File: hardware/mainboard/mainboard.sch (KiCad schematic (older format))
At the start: 1 part, among them J1 2309407-1

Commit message: displays done, sd card and camera is left
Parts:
- added C?: 10nF, symbol Device:C_Small
- added C?: 4.7uF, symbol Device:C_Small
- added C?: 10uF, symbol Device:C_Small
- added J?: Micro_SD_Card_Det, symbol Connector:Micro_SD_Card_Det
- added JP? (x2): BL_SELECT, symbol Jumper:SolderJumper_3_Open
- added U?: MCP1725-3302E_SN, SOIC127P599X175-8N, symbol mainboard:MCP1725-3302E_SN
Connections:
- net labels added: GPIO_BL, LED_3V, MIPI_RX0_CLKN, MIPI_RX0_CLKP, MIPI_RX0_D0N, MIPI_RX0_D0P, MIPI_RX0_D1N, MIPI_RX0_D1P, MIPI_RX0_D2N, MIPI_RX0_D2P, MIPI_RX0_D3N, MIPI_RX0_D3P, MIPI_TX0_CLKN, MIPI_TX0_CLKP, MIPI_TX0_D0N, MIPI_TX0_D0P, MIPI_TX0_D1N, MIPI_TX0_D1P, MIPI_TX0_D2N, MIPI_TX0_D2P, MIPI_TX0_D3N, MIPI_TX0_D3P, MIPI_TX1_CLKN, MIPI_TX1_CLKP, MIPI_TX1_D0N, MIPI_TX1_D0P, MIPI_TX1_D1N, MIPI_TX1_D1P, MIPI_TX1_D2N, MIPI_TX1_D2P, MIPI_TX1_D3N, MIPI_TX1_D3P, RESX_0, RESX_1
- wire segments 21 -> 99
- no-connect marks 0 -> 1
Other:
- note added: "HDMI\n"
- note added: "MIPI CSI0"
- note added: "MIPI CSI0\n"
- note added: "MIPI DSI0"
- note added: "MIPI DSI1"
- note added: "MIPI DSI1\n"
- moved on the sheet: J1A, J1B

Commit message: finished camera, sd, imu, power supplies, might be done with schematic
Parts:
- removed C?: 10nF, symbol Device:C_Small
- removed C?: 4.7uF, symbol Device:C_Small
- removed C?: 10uF, symbol Device:C_Small
- removed J?: Micro_SD_Card_Det, symbol Connector:Micro_SD_Card_Det
- removed U?: MCP1725-3302E_SN, SOIC127P599X175-8N, symbol mainboard:MCP1725-3302E_SN
- added C10, C12, C8: 100nF, symbol Device:C_Small
- added C11: 4.7uF, symbol Device:C_Small
- added C13, C6, C7: 1uF, symbol Device:C_Small
- added C9, C?: 10nF, symbol Device:C_Small
- added C? (x2): 0.1uF, symbol Device:C_Small
- added C?: 2.2uF, symbol Device:C_Small
- added J3: Conn_01x02_Male, symbol Connector:Conn_01x02_Male
- added J4: AXK7L24223G, PANASONIC_AXK7L24223G, symbol mainboard:AXK7L24223G
- added J5: 503182-1852, MOLEX_503182-1852, symbol mainboard:503182-1852
- added R1: 60k, symbol Device:R_Small_US
- added R2: 10k, symbol Device:R_Small_US
- added TP1, TP2, TP3, TP4: TestPoint, symbol Connector:TestPoint
- added U2: MIC5504-1.2YM5-TR, SOT23-5P95_280X145XL45X37N, symbol mainboard:MIC5504-1.2YM5-TR
- added U3: MCP1725-ADJE_MC, SOIC127P599X175-8N, symbol mainboard:MCP1725-ADJE_MC
- added U?: ICM-20602, PQFN50P300X300X80-16N, symbol mainboard:ICM-20602
- gave numbers to parts that had none: 2
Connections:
- net labels added: +1V2, +2V8, GPIO2_B3_CIF_CLKOUTA, I2C1_SCL, I2C1_SDA, I2C2_SCL, I2C2_SDA, MIPI_CSI0_PWN, MIPI_CSI1_RST
- net labels removed: LED_3V
- wire segments 99 -> 132
- no-connect marks 1 -> 5
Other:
- note added: "(this is hella sus)"
- note added: "Camera digital core regulator\n"
- note added: "OV13850 B2B Conn\n"
- note added: "microSD\n"
- moved on the sheet: J1B

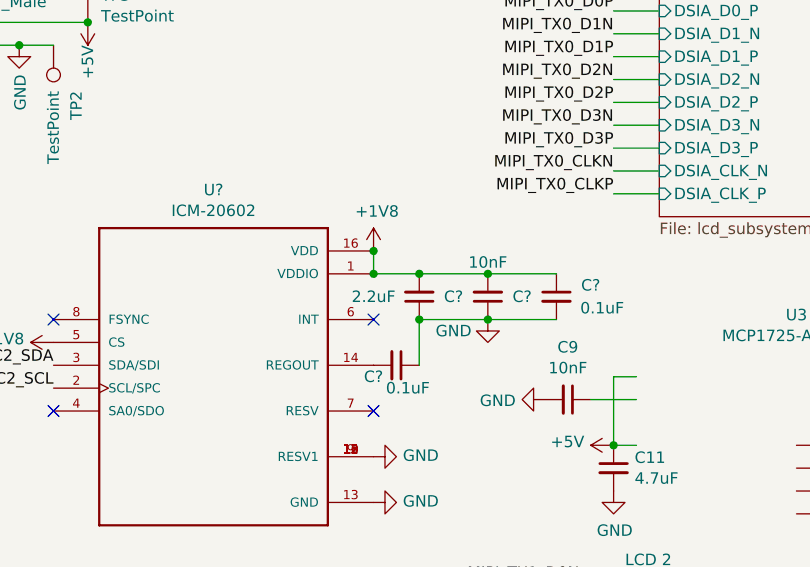
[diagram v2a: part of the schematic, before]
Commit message: footprints assigned, ready to begin pcb design
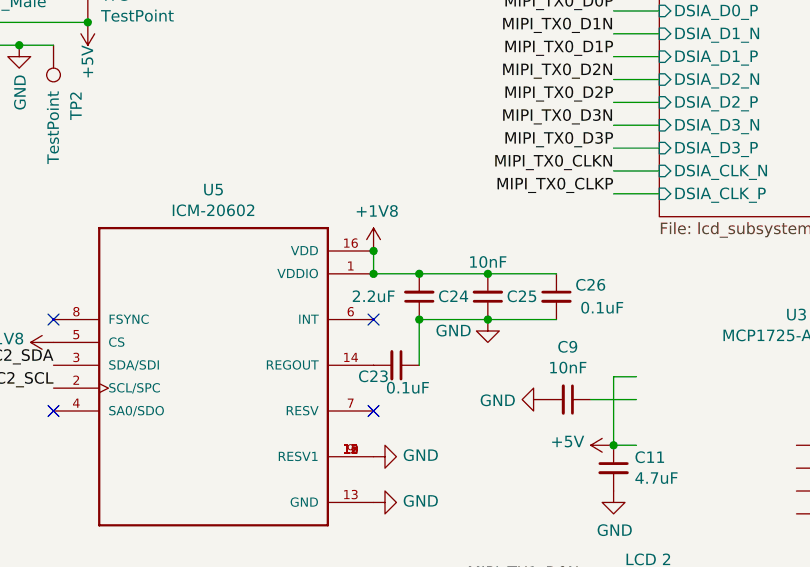
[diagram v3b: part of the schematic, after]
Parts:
- C10, C11, C12, C13, C6, C7, C8, C9: footprint (none) -> Capacitor_SMD:C_0603_1608Metric_Pad1.08x0.95mm_HandSolder
- C23, C24, C25, C26: renamed from C?; footprint (none) -> Capacitor_SMD:C_0603_1608Metric_Pad1.08x0.95mm_HandSolder
- J3: footprint (none) -> Connector_PinHeader_2.54mm:PinHeader_1x02_P2.54mm_Vertical
- J4: footprint PANASONIC_AXK7L24223G -> mainboard:PANASONIC_AXK7L24223G
- J5: footprint MOLEX_503182-1852 -> mainboard:MOLEX_503182-1852
- JP1, JP2: footprint (none) -> Jumper:SolderJumper-3_P1.3mm_Open_Pad1.0x1.5mm
- R1, R2: footprint (none) -> Resistor_SMD:R_0603_1608Metric_Pad0.98x0.95mm_HandSolder
- TP1, TP2, TP3, TP4: footprint (none) -> TestPoint:TestPoint_Pad_2.5x2.5mm
- U2: footprint SOT23-5P95_280X145XL45X37N -> mainboard:SOT23-5P95_280X145XL45X37N
- U3: footprint SOIC127P599X175-8N -> mainboard:SOIC127P599X175-8N
- U5: renamed from U?; footprint PQFN50P300X300X80-16N -> mainboard:PQFN50P300X300X80-16N
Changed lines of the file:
@@
 F 0 "JP1" V 10754 1318 50  0000 L CNN
 F 1 "BL_SELECT" V 10845 1318 50  0000 L CNN
-F 2 "" H 10800 1250 50  0001 C CNN
+F 2 "Jumper:SolderJumper-3_P1.3mm_Open_Pad1.0x1.5mm" H 10800 1250 50  0001 C CNN
 F 3 "~" H 10800 1250 50  0001 C CNN
 	1    10800 1250
@@
 F 0 "JP2" V 10604 3918 50  0000 L CNN
 F 1 "BL_SELECT" V 10695 3918 50  0000 L CNN
-F 2 "" H 10650 3850 50  0001 C CNN
+F 2 "Jumper:SolderJumper-3_P1.3mm_Open_Pad1.0x1.5mm" H 10650 3850 50  0001 C CNN
 F 3 "~" H 10650 3850 50  0001 C CNN
 	1    10650 3850
@@
 F 0 "J5" H 10580 5696 50  0000 L CNN
 F 1 "503182-1852" H 10580 5605 50  0000 L CNN
-F 2 "MOLEX_503182-1852" H 10050 5650 50  0001 L BNN
+F 2 "mainboard:MOLEX_503182-1852" H 10050 5650 50  0001 L BNN
 F 3 "Molex" H 10050 5650 50  0001 L BNN
 	1    10050 5650
@@
 F 0 "J4" H 7700 6217 50  0000 C CNN
 F 1 "AXK7L24223G" H 7700 6126 50  0000 C CNN
-F 2 "PANASONIC_AXK7L24223G" H 7700 5450 50  0001 L BNN
+F 2 "mainboard:PANASONIC_AXK7L24223G" H 7700 5450 50  0001 L BNN
 F 3 "Panasonic" H 7700 5450 50  0001 L BNN
 	1    7700 5450
@@
 F 0 "U3" H 9900 3170 50  0000 C CNN
 F 1 "MCP1725-ADJE_MC" H 9900 3079 50  0000 C CNN
-F 2 "SOIC127P599X175-8N" H 9900 2600 50  0001 L BNN
+F 2 "mainboard:SOIC127P599X175-8N" H 9900 2600 50  0001 L BNN
 F 3 "" H 9900 2600 50  0001 C CNN
 	1    9900 2600
@@
 F 0 "C9" V 8671 2400 50  0000 C CNN
 F 1 "10nF" V 8762 2400 50  0000 C CNN
-F 2 "" H 8900 2400 50  0001 C CNN
+F 2 "Capacitor_SMD:C_0603_1608Metric_Pad1.08x0.95mm_HandSolder" H 8900 2400 50  0001 C CNN
 F 3 "~" H 8900 2400 50  0001 C CNN
 	1    8900 2400
@@
 F 0 "C11" H 9192 2746 50  0000 L CNN
 F 1 "4.7uF" H 9192 2655 50  0000 L CNN
-F 2 "" H 9100 2700 50  0001 C CNN
+F 2 "Capacitor_SMD:C_0603_1608Metric_Pad1.08x0.95mm_HandSolder" H 9100 2700 50  0001 C CNN
 F 3 "~" H 9100 2700 50  0001 C CNN
 	1    9100 2700
@@
 F 0 "C13" H 10650 2350 50  0000 C CNN
 F 1 "1uF" H 10650 2250 50  0000 C CNN
-F 2 "" H 10800 2300 50  0001 C CNN
+F 2 "Capacitor_SMD:C_0603_1608Metric_Pad1.08x0.95mm_HandSolder" H 10800 2300 50  0001 C CNN
 F 3 "~" H 10800 2300 50  0001 C CNN
 	1    10800 2300
@@
 F 0 "C8" H 8692 4846 50  0000 L CNN
 F 1 "100nF" H 8692 4755 50  0000 L CNN
-F 2 "" H 8600 4800 50  0001 C CNN
+F 2 "Capacitor_SMD:C_0603_1608Metric_Pad1.08x0.95mm_HandSolder" H 8600 4800 50  0001 C CNN
 F 3 "~" H 8600 4800 50  0001 C CNN
 	1    8600 4800
@@
 F 0 "C10" H 9092 4846 50  0000 L CNN
 F 1 "100nF" H 9092 4755 50  0000 L CNN
-F 2 "" H 9000 4800 50  0001 C CNN
+F 2 "Capacitor_SMD:C_0603_1608Metric_Pad1.08x0.95mm_HandSolder" H 9000 4800 50  0001 C CNN
 F 3 "~" H 9000 4800 50  0001 C CNN
 	1    9000 4800
@@
 F 0 "C12" H 10842 5296 50  0000 L CNN
 F 1 "100nF" H 10842 5205 50  0000 L CNN
-F 2 "" H 10750 5250 50  0001 C CNN
+F 2 "Capacitor_SMD:C_0603_1608Metric_Pad1.08x0.95mm_HandSolder" H 10750 5250 50  0001 C CNN
 F 3 "~" H 10750 5250 50  0001 C CNN
 	1    10750 5250
@@
 F 0 "R1" H 10768 2596 50  0000 L CNN
 F 1 "60k" H 10768 2505 50  0000 L CNN
-F 2 "" H 10700 2550 50  0001 C CNN
+F 2 "Resistor_SMD:R_0603_1608Metric_Pad0.98x0.95mm_HandSolder" H 10700 2550 50  0001 C CNN
 F 3 "~" H 10700 2550 50  0001 C CNN
 	1    10700 2550
@@
 F 0 "R2" H 10768 2796 50  0000 L CNN
 F 1 "10k" H 10768 2705 50  0000 L CNN
-F 2 "" H 10700 2750 50  0001 C CNN
+F 2 "Resistor_SMD:R_0603_1608Metric_Pad0.98x0.95mm_HandSolder" H 10700 2750 50  0001 C CNN
 F 3 "~" H 10700 2750 50  0001 C CNN
 	1    10700 2750
@@
 F 0 "J3" H 6308 931 50  0000 C CNN
 F 1 "Conn_01x02_Male" H 6308 840 50  0000 C CNN
-F 2 "" H 6200 750 50  0001 C CNN
+F 2 "Connector_PinHeader_2.54mm:PinHeader_1x02_P2.54mm_Vertical" H 6200 750 50  0001 C CNN
 F 3 "~" H 6200 750 50  0001 C CNN
 	1    6200 750
@@
 F 0 "U2" H 7250 4467 50  0000 C CNN
 F 1 "MIC5504-1.2YM5-TR" H 7250 4376 50  0000 C CNN
-F 2 "SOT23-5P95_280X145XL45X37N" H 7250 4000 50  0001 L BNN
+F 2 "mainboard:SOT23-5P95_280X145XL45X37N" H 7250 4000 50  0001 L BNN
 F 3 "MICREL" H 7250 4000 50  0001 L BNN
 	1    7250 4000
@@
 F 0 "C6" H 7500 3700 50  0000 C CNN
 F 1 "1uF" H 7650 3700 50  0000 C CNN
-F 2 "" H 7800 3700 50  0001 C CNN
+F 2 "Capacitor_SMD:C_0603_1608Metric_Pad1.08x0.95mm_HandSolder" H 7800 3700 50  0001 C CNN
 F 3 "~" H 7800 3700 50  0001 C CNN
 	1    7800 3700
@@
 F 0 "C7" H 7750 4150 50  0000 C CNN
 F 1 "1uF" H 7750 4050 50  0000 C CNN
-F 2 "" H 7900 4100 50  0001 C CNN
+F 2 "Capacitor_SMD:C_0603_1608Metric_Pad1.08x0.95mm_HandSolder" H 7900 4100 50  0001 C CNN
 F 3 "~" H 7900 4100 50  0001 C CNN
 	1    7900 4100
@@
 F 0 "TP3" H 6858 868 50  0000 L CNN
 F 1 "TestPoint" H 6858 777 50  0000 L CNN
-F 2 "" H 7000 750 50  0001 C CNN
+F 2 "TestPoint:TestPoint_Pad_2.5x2.5mm" H 7000 750 50  0001 C CNN
 F 3 "~" H 7000 750 50  0001 C CNN
 	1    6800 750
@@
 F 0 "TP2" V 6550 1050 50  0000 L CNN
 F 1 "TestPoint" V 6650 1050 50  0000 L CNN
-F 2 "" H 6850 850 50  0001 C CNN
+F 2 "TestPoint:TestPoint_Pad_2.5x2.5mm" H 6850 850 50  0001 C CNN
 F 3 "~" H 6850 850 50  0001 C CNN
 	1    6650 850
@@
 F 0 "TP1" H 6442 4126 50  0000 R CNN
 F 1 "TestPoint" H 6442 4217 50  0000 R CNN
-F 2 "" H 6700 4100 50  0001 C CNN
+F 2 "TestPoint:TestPoint_Pad_2.5x2.5mm" H 6700 4100 50  0001 C CNN
 F 3 "~" H 6700 4100 50  0001 C CNN
 	1    6500 4100
@@
 F 0 "TP4" H 10658 2068 50  0000 L CNN
 F 1 "TestPoint" H 10658 1977 50  0000 L CNN
-F 2 "" H 10800 1950 50  0001 C CNN
+F 2 "TestPoint:TestPoint_Pad_2.5x2.5mm" H 10800 1950 50  0001 C CNN
 F 3 "~" H 10800 1950 50  0001 C CNN
 	1    10600 1950
@@
 	8050 1750 8050 1850
 $Comp
-L power:GND #PWR?
+L power:GND #PWR0268
 U 1 1 60619FA8
 P 8050 2850
-F 0 "#PWR?" H 8050 2600 50  0001 C CNN
+F 0 "#PWR0268" H 8050 2600 50  0001 C CNN
 F 1 "GND" V 8055 2722 50  0000 R CNN
 F 2 "" H 8050 2850 50  0001 C CNN
@@
 $EndComp
 $Comp
-L mainboard:ICM-20602 U?
+L mainboard:ICM-20602 U5
 U 1 1 604B17B1
 P 7350 2250
-F 0 "U?" H 7350 3017 50  0000 C CNN
+F 0 "U5" H 7350 3017 50  0000 C CNN
 F 1 "ICM-20602" H 7350 2926 50  0000 C CNN
-F 2 "PQFN50P300X300X80-16N" H 7350 2250 50  0001 L BNN
+F 2 "mainboard:PQFN50P300X300X80-16N" H 7350 2250 50  0001 L BNN
 F 3 "World's Best 6-Axis Integrated s" H 7350 2250 50  0001 L BNN
 F 4 "Unavailable" H 7350 2250 50  0001 L BNN "Field4"
@@
 NoConn ~ 8050 2450
 $Comp
-L power:GND #PWR?
+L power:GND #PWR0269
 U 1 1 6062A11D
 P 8050 2650
-F 0 "#PWR?" H 8050 2400 50  0001 C CNN
+F 0 "#PWR0269" H 8050 2400 50  0001 C CNN
 F 1 "GND" V 8055 2522 50  0000 R CNN
 F 2 "" H 8050 2650 50  0001 C CNN
@@
 $EndComp
 $Comp
-L Device:C_Small C?
+L Device:C_Small C26
 U 1 1 60637F47
 P 8850 1950
-F 0 "C?" H 9000 2000 50  0000 C CNN
+F 0 "C26" H 9000 2000 50  0000 C CNN
 F 1 "0.1uF" H 9050 1900 50  0000 C CNN
-F 2 "" H 8850 1950 50  0001 C CNN
+F 2 "Capacitor_SMD:C_0603_1608Metric_Pad1.08x0.95mm_HandSolder" H 8850 1950 50  0001 C CNN
 F 3 "~" H 8850 1950 50  0001 C CNN
 	1    8850 1950
@@
 $EndComp
 $Comp
-L Device:C_Small C?
+L Device:C_Small C24
 U 1 1 60654A5D
 P 8250 1950
-F 0 "C?" H 8100 1950 50  0000 C CNN
+F 0 "C24" H 8100 1950 50  0000 C CNN
 F 1 "2.2uF" H 8450 1950 50  0000 C CNN
-F 2 "" H 8250 1950 50  0001 C CNN
+F 2 "Capacitor_SMD:C_0603_1608Metric_Pad1.08x0.95mm_HandSolder" H 8250 1950 50  0001 C CNN
 F 3 "~" H 8250 1950 50  0001 C CNN
 	1    8250 1950
@@
 $EndComp
 $Comp
-L Device:C_Small C?
+L Device:C_Small C25
 U 1 1 60656CBF
 P 8550 1950
-F 0 "C?" H 8400 1950 50  0000 C CNN
+F 0 "C25" H 8400 1950 50  0000 C CNN
 F 1 "10nF" H 8550 1800 50  0000 C CNN
-F 2 "" H 8550 1950 50  0001 C CNN
+F 2 "Capacitor_SMD:C_0603_1608Metric_Pad1.08x0.95mm_HandSolder" H 8550 1950 50  0001 C CNN
 F 3 "~" H 8550 1950 50  0001 C CNN
 	1    8550 1950
@@
 	8250 2050 8550 2050
 $Comp
-L power:GND #PWR?
+L power:GND #PWR0270
 U 1 1 60671A65
 P 8550 2050
-F 0 "#PWR?" H 8550 1800 50  0001 C CNN
+F 0 "#PWR0270" H 8550 1800 50  0001 C CNN
 F 1 "GND" H 8400 2000 50  0000 C CNN
 F 2 "" H 8550 2050 50  0001 C CNN
@@
 NoConn ~ 8050 2050
 $Comp
-L Device:C_Small C?
+L Device:C_Small C23
 U 1 1 606AE30E
 P 8150 2250
-F 0 "C?" V 8200 2150 50  0000 C CNN
+F 0 "C23" V 8200 2150 50  0000 C CNN
 F 1 "0.1uF" V 8250 2300 50  0000 C CNN
-F 2 "" H 8150 2250 50  0001 C CNN
+F 2 "Capacitor_SMD:C_0603_1608Metric_Pad1.08x0.95mm_HandSolder" H 8150 2250 50  0001 C CNN
 F 3 "~" H 8150 2250 50  0001 C CNN
 	1    8150 2250
@@
 	8550 2050 8850 2050
 $Comp
-L power:+1V8 #PWR?
+L power:+1V8 #PWR0271
 U 1 1 60780DF4
 P 6650 2150
-F 0 "#PWR?" H 6650 2000 50  0001 C CNN
+F 0 "#PWR0271" H 6650 2000 50  0001 C CNN
 F 1 "+1V8" V 6665 2278 50  0000 L CNN
 F 2 "" H 6650 2150 50  0001 C CNN
@@
 NoConn ~ 6650 2050
 $Comp
-L power:+1V8 #PWR?
+L power:+1V8 #PWR0272
 U 1 1 607F967D
 P 8050 1750
-F 0 "#PWR?" H 8050 1600 50  0001 C CNN
+F 0 "#PWR0272" H 8050 1600 50  0001 C CNN
 F 1 "+1V8" H 8065 1923 50  0000 C CNN
 F 2 "" H 8050 1750 50  0001 C CNN

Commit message: mipi done, power almost done
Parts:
- removed TP2: TestPoint, TestPoint:TestPoint_Pad_2.5x2.5mm, symbol Connector:TestPoint
- added H1, H2, H3, H4: MountingHole, MountingHole:MountingHole_2.2mm_M2_Pad_Via, symbol Mechanical:MountingHole
- C10, C11, C12, C13, C23, C24, C25, C26, C6, C7, C8, C9: footprint Capacitor_SMD:C_0603_1608Metric_Pad1.08x0.95mm_HandSolder -> Capacitor_SMD:C_0402_1005Metric_Pad0.74x0.62mm_HandSolder
- R1, R2: footprint Resistor_SMD:R_0603_1608Metric_Pad0.98x0.95mm_HandSolder -> Resistor_SMD:R_0402_1005Metric_Pad0.72x0.64mm_HandSolder
- TP1, TP3, TP4: footprint TestPoint:TestPoint_Pad_2.5x2.5mm -> TestPoint:TestPoint_Pad_D1.0mm
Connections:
- net labels added: MIPI_RX0_CLK+, MIPI_RX0_CLK-, MIPI_RX0_D0+, MIPI_RX0_D0-, MIPI_RX0_D1+, MIPI_RX0_D1-, MIPI_RX0_D2+, MIPI_RX0_D2-, MIPI_RX0_D3+, MIPI_RX0_D3-, MIPI_TX0_CLK+, MIPI_TX0_CLK-, MIPI_TX0_D0+, MIPI_TX0_D0-, MIPI_TX0_D1+, MIPI_TX0_D1-, MIPI_TX0_D2+, MIPI_TX0_D2-, MIPI_TX0_D3+, MIPI_TX0_D3-, MIPI_TX1_CLK+, MIPI_TX1_CLK-, MIPI_TX1_D0+, MIPI_TX1_D0-, MIPI_TX1_D1+, MIPI_TX1_D1-, MIPI_TX1_D2+, MIPI_TX1_D2-, MIPI_TX1_D3+, MIPI_TX1_D3-
- net labels removed: MIPI_RX0_CLKN, MIPI_RX0_CLKP, MIPI_RX0_D0N, MIPI_RX0_D0P, MIPI_RX0_D1N, MIPI_RX0_D1P, MIPI_RX0_D2N, MIPI_RX0_D2P, MIPI_RX0_D3N, MIPI_RX0_D3P, MIPI_TX0_CLKN, MIPI_TX0_CLKP, MIPI_TX0_D0N, MIPI_TX0_D0P, MIPI_TX0_D1N, MIPI_TX0_D1P, MIPI_TX0_D2N, MIPI_TX0_D2P, MIPI_TX0_D3N, MIPI_TX0_D3P, MIPI_TX1_CLKN, MIPI_TX1_CLKP, MIPI_TX1_D0N, MIPI_TX1_D0P, MIPI_TX1_D1N, MIPI_TX1_D1P, MIPI_TX1_D2N, MIPI_TX1_D2P, MIPI_TX1_D3N, MIPI_TX1_D3P
- wire segments 132 -> 131

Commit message: 0.1 routing done, will merge after cleaning up silkscreen
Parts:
- removed JP1, JP2: BL_SELECT, Jumper:SolderJumper-3_P1.3mm_Open_Pad1.0x1.5mm, symbol Jumper:SolderJumper_3_Open
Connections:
- net labels removed: +12V
- no-connect marks 5 -> 13
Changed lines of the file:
@@
 DDR4 SODIMM Connector 260pin\n
-$Comp
-L power:+12V #PWR0101
-U 1 1 5F871C09
-P 1750 900
-F 0 "#PWR0101" H 1750 750 50  0001 C CNN
-F 1 "+12V" V 1765 1028 50  0000 L CNN
-F 2 "" H 1750 900 50  0001 C CNN
-F 3 "" H 1750 900 50  0001 C CNN
-	1    1750 900
-	0    -1   -1   0
-$EndComp
-$Comp
-L power:+12V #PWR0102
-U 1 1 5F872FCD
-P 1750 1000
-F 0 "#PWR0102" H 1750 850 50  0001 C CNN
-F 1 "+12V" V 1765 1128 50  0000 L CNN
-F 2 "" H 1750 1000 50  0001 C CNN
-F 3 "" H 1750 1000 50  0001 C CNN
-	1    1750 1000
-	0    -1   -1   0
-$EndComp
-$Comp
-L power:+12V #PWR0103
-U 1 1 5F874932
-P 1750 1100
-F 0 "#PWR0103" H 1750 950 50  0001 C CNN
-F 1 "+12V" V 1765 1228 50  0000 L CNN
-F 2 "" H 1750 1100 50  0001 C CNN
-F 3 "" H 1750 1100 50  0001 C CNN
-	1    1750 1100
-	0    -1   -1   0
-$EndComp
-$Comp
-L power:+12V #PWR0104
-U 1 1 5F874938
-P 1750 1200
-F 0 "#PWR0104" H 1750 1050 50  0001 C CNN
-F 1 "+12V" V 1765 1328 50  0000 L CNN
-F 2 "" H 1750 1200 50  0001 C CNN
-F 3 "" H 1750 1200 50  0001 C CNN
-	1    1750 1200
-	0    -1   -1   0
-$EndComp
-$Comp
-L mainboard:2309407-1 J1
-U 1 1 5F89D220
-P 2250 4300
-F 0 "J1" H 2250 7967 50  0000 C CNN
-F 1 "2309407-1" H 2250 7876 50  0000 C CNN
-F 2 "mainboard:TE_2309407-1" H 2250 4300 50  0001 L BNN
-F 3 "Socket" H 2250 4300 50  0001 L BNN
-F 4 "2309407-1" H 2250 4300 50  0001 L BNN "Field4"
-F 5 "Compliant" H 2250 4300 50  0001 L BNN "Field5"
-F 6 ".5 mm[.0197 in]" H 2250 4300 50  0001 L BNN "Field6"
-F 7 "260" H 2250 4300 50  0001 L BNN "Field7"
-	1    2250 4300
-	1    0    0    -1
-$EndComp
 $Comp
 L power:GND #PWR0105
@@
 	1    2750 1400
 	0    -1   -1   0
-$EndComp
-$Comp
-L power:+12V #PWR0173
-U 1 1 5F8E37A4
-P 2750 900
-F 0 "#PWR0173" H 2750 750 50  0001 C CNN
-F 1 "+12V" V 2765 1028 50  0000 L CNN
-F 2 "" H 2750 900 50  0001 C CNN
-F 3 "" H 2750 900 50  0001 C CNN
-	1    2750 900
-	0    1    1    0
-$EndComp
-$Comp
-L power:+12V #PWR0174
-U 1 1 5F8E6A05
-P 2750 1000
-F 0 "#PWR0174" H 2750 850 50  0001 C CNN
-F 1 "+12V" V 2765 1128 50  0000 L CNN
-F 2 "" H 2750 1000 50  0001 C CNN
-F 3 "" H 2750 1000 50  0001 C CNN
-	1    2750 1000
-	0    1    1    0
-$EndComp
-$Comp
-L power:+12V #PWR0175
-U 1 1 5F8E6FBE
-P 2750 1100
-F 0 "#PWR0175" H 2750 950 50  0001 C CNN
-F 1 "+12V" V 2765 1228 50  0000 L CNN
-F 2 "" H 2750 1100 50  0001 C CNN
-F 3 "" H 2750 1100 50  0001 C CNN
-	1    2750 1100
-	0    1    1    0
-$EndComp
-$Comp
-L power:+12V #PWR0176
-U 1 1 5F8E754A
-P 2750 1200
-F 0 "#PWR0176" H 2750 1050 50  0001 C CNN
-F 1 "+12V" V 2765 1328 50  0000 L CNN
-F 2 "" H 2750 1200 50  0001 C CNN
-F 3 "" H 2750 1200 50  0001 C CNN
-	1    2750 1200
-	0    1    1    0
 $EndComp
 $Comp
@@
 Wire Wire Line
 	10350 3850 10500 3850
-Text Label 10650 3650 0    50   ~ 0
-PWM0_BL
 Wire Wire Line
 	10500 1250 10650 1250
-Text Label 10800 1050 0    50   ~ 0
-PWM0_BL
 Wire Wire Line
 	10350 3350 10500 3350
-$Comp
-L Jumper:SolderJumper_3_Open JP1
-U 1 1 5FBE2450
-P 10800 1250
-F 0 "JP1" V 10754 1318 50  0000 L CNN
-F 1 "BL_SELECT" V 10845 1318 50  0000 L CNN
-F 2 "Jumper:SolderJumper-3_P1.3mm_Open_Pad1.0x1.5mm" H 10800 1250 50  0001 C CNN
-F 3 "~" H 10800 1250 50  0001 C CNN
-	1    10800 1250
-	0    1    1    0
-$EndComp
-$Comp
-L Jumper:SolderJumper_3_Open JP2
-U 1 1 5FBF2B1E
-P 10650 3850
-F 0 "JP2" V 10604 3918 50  0000 L CNN
-F 1 "BL_SELECT" V 10695 3918 50  0000 L CNN
-F 2 "Jumper:SolderJumper-3_P1.3mm_Open_Pad1.0x1.5mm" H 10650 3850 50  0001 C CNN
-F 3 "~" H 10650 3850 50  0001 C CNN
-	1    10650 3850
-	0    1    1    0
-$EndComp
 Text Label 1750 2900 2    50   ~ 0
 GPIO_BL
-Text Label 10800 1450 3    50   ~ 0
+Text Label 10650 1250 0    50   ~ 0
 GPIO_BL
-Text Label 10650 4050 3    50   ~ 0
+Text Label 10500 3850 0    50   ~ 0
 GPIO_BL
 Text Label 8950 3200 2    50   ~ 0
@@
 	1450 3600 1750 3600
 Text Label 7300 5050 2    50   ~ 0
-I2C1_SCL
+I2C2_SCL
 Text Label 7300 4950 2    50   ~ 0
-I2C1_SDA
+I2C2_SDA
 Text Label 1400 6400 2    50   ~ 0
 GPIO2_B3_CIF_CLKOUTA
@@
 $EndComp
 $Comp
-L power:+5V #PWR0254
-U 1 1 602EBB93
-P 6800 750
-F 0 "#PWR0254" H 6800 600 50  0001 C CNN
-F 1 "+5V" V 6800 850 50  0000 L CNN
-F 2 "" H 6800 750 50  0001 C CNN
-F 3 "" H 6800 750 50  0001 C CNN
-	1    6800 750
-	-1   0    0    1
-$EndComp
-$Comp
 L mainboard:MIC5504-1.2YM5-TR U2
 U 1 1 60318263
@@
 Wire Wire Line
 	6400 750  6800 750
-Connection ~ 6800 750
 Wire Wire Line
 	6400 850  6500 850
@@
 	1450 3800 1750 3800
 Text Label 6650 2350 2    50   ~ 0
-I2C2_SCL
+I2C1_SCL
 Text Label 6650 2250 2    50   ~ 0
-I2C2_SDA
+I2C1_SDA
 NoConn ~ 6650 2450
 NoConn ~ 6650 2050
@@
 	0    -1   -1   0
 $EndComp
+$Comp
+L power:+3.3V #PWR0254
+U 1 1 5FA847B9
+P 6800 750
+F 0 "#PWR0254" H 6800 600 50  0001 C CNN
+F 1 "+3.3V" H 6815 923 50  0000 C CNN
+F 2 "" H 6800 750 50  0001 C CNN
+F 3 "" H 6800 750 50  0001 C CNN
+	1    6800 750
+	-1   0    0    1
+$EndComp
+Connection ~ 6800 750
+$Comp
+L mainboard:2309407-1 J1
+U 1 1 5F89D220
+P 2250 4300
+F 0 "J1" H 2250 7967 50  0000 C CNN
+F 1 "2309407-1" H 2250 7876 50  0000 C CNN
+F 2 "mainboard:TE_2309407-1" H 2250 4300 50  0001 L BNN
+F 3 "Socket" H 2250 4300 50  0001 L BNN
+F 4 "2309407-1" H 2250 4300 50  0001 L BNN "Field4"
+F 5 "Compliant" H 2250 4300 50  0001 L BNN "Field5"
+F 6 ".5 mm[.0197 in]" H 2250 4300 50  0001 L BNN "Field6"
+F 7 "260" H 2250 4300 50  0001 L BNN "Field7"
+	1    2250 4300
+	1    0    0    -1
+$EndComp
+NoConn ~ 1750 900
+NoConn ~ 1750 1000
+NoConn ~ 1750 1100
+NoConn ~ 1750 1200
+NoConn ~ 2750 900
+NoConn ~ 2750 1000
+NoConn ~ 2750 1100
+NoConn ~ 2750 1200
 $EndSCHEMATC
